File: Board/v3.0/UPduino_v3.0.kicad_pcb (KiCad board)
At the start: 4 copper layers, 62 x 22.2 mm, 113 parts, among them J1 47589-0001, J2 Right, J3 Left, J4 5V Power, U1 93LC56BT-I/OT, U2 ICE40UP5K-SG48ITR, U3 FT232H, U4 SG-210STF 12.0000ML3, U5 W25Q32JVSSIM, U6 AP2127K-3.3, U7 AP2127K-1.2, U8 SN74AUP2G125DCUR

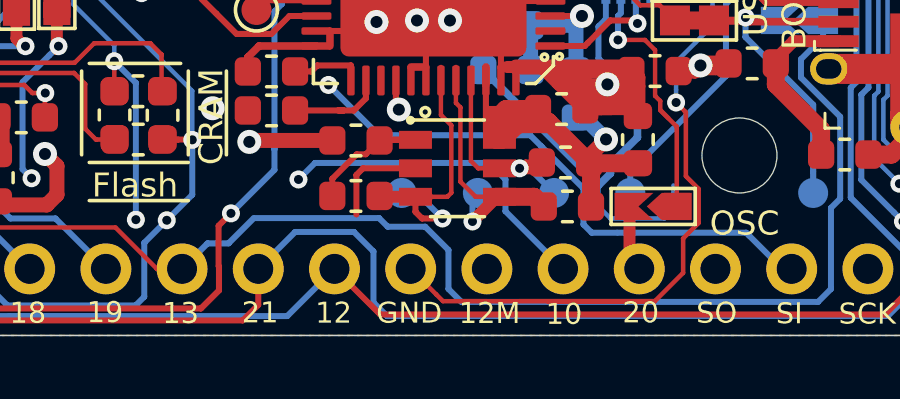
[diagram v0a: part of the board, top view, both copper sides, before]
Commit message: Modified silkscreen and updated gerbers. Used for final production run
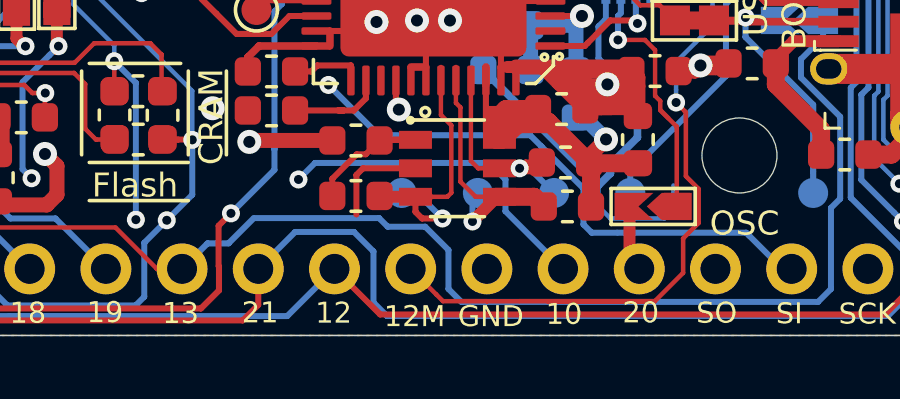
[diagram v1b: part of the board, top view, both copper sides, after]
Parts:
- added G***: LOGO, Logos:Logo_silk_ROHS_10x5.6mm, B.Cu at (135.8, 84.1)
- added REF**: ESD-Logo_6.6x6mm_SilkScreen, Symbol:ESD-Logo_6.6x6mm_SilkScreen, B.Cu at (129.8, 89.2)
- moved REF** 2.55 mm to (138.0, 90.6)

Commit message: Changed schematic to reflect shorted and open jumpers
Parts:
- removed the G*** at (135.8, 84.1)
- removed the REF** at (129.8, 89.2)
- R22, R23: value JUMPER -> OPEN
- R28: value JUMPER -> SHORT
- SJ16: renamed from R16; value JUMPER -> OPEN
- SJ19: renamed from R19; value JUMPER -> OPEN
- SJ20: renamed from R20; value JUMPER -> SHORT
- SJ24: renamed from R24; value JUMPER -> OPEN
- SJ25: renamed from R25; value JUMPER -> OPEN
- SJ26: renamed from R26; value JUMPER -> OPEN
- SJ31: renamed from R31; value JUMPER -> SHORT
- SJ34: renamed from R34; value JUMPER -> SHORT
- SJ35: renamed from R35; value JUMPER -> SHORT
- SJ36: renamed from R36; value JUMPER -> SHORT
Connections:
- U3 pad 49: GND -> (no net)
